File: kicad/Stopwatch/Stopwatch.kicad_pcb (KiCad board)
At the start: 2 copper layers, 13 parts, among them U1 74HC14, U3 SC56-11GWA, U4 SC56-11GWA, U5 SC56-11GWA, U6 SC56-11GWA

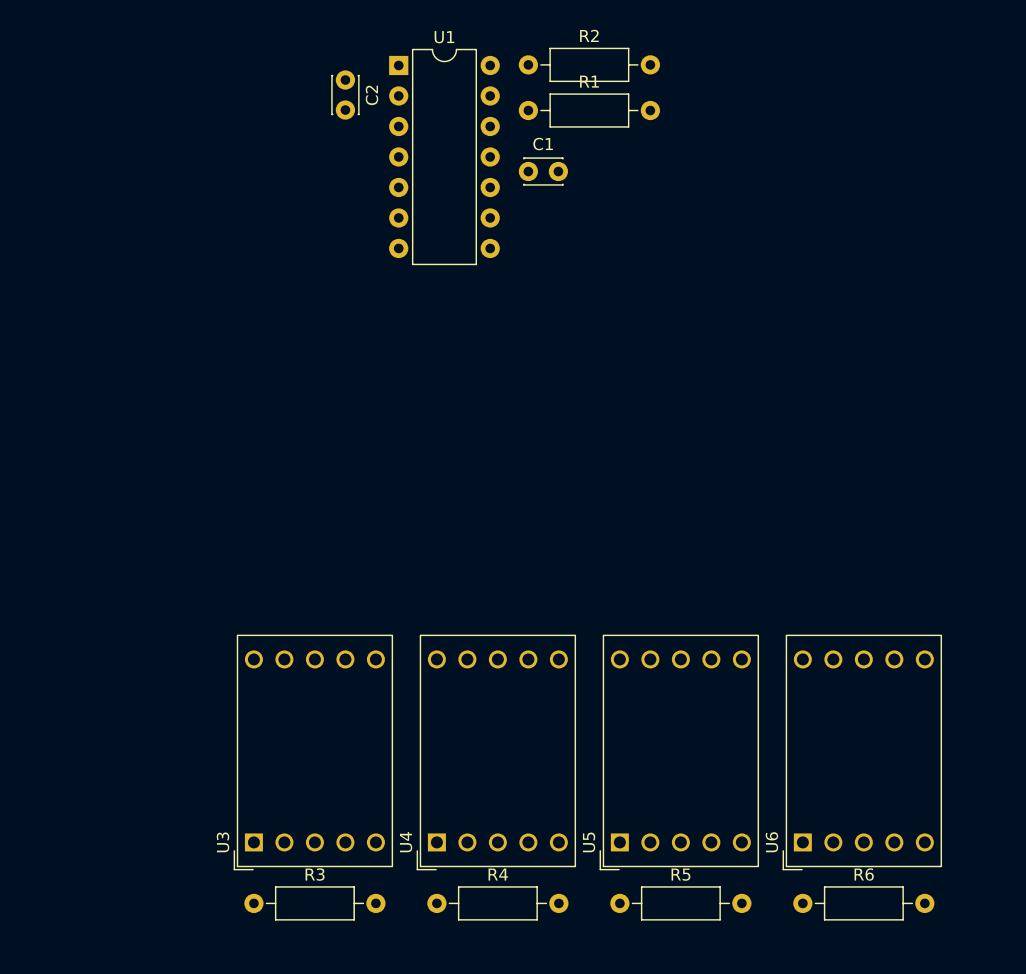
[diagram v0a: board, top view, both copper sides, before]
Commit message: fixed BluePill symbol pin numbers, added button and BluePill footprint
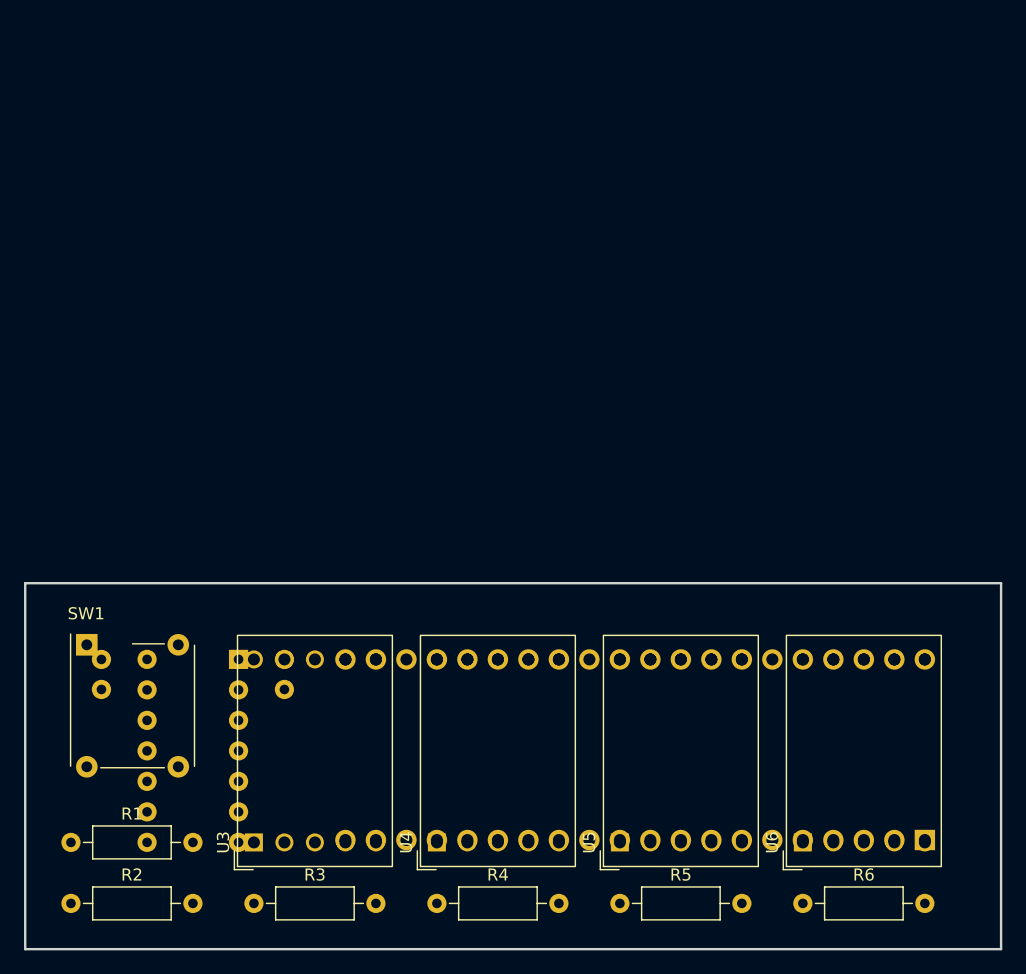
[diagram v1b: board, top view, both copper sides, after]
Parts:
- added SW1: SW_Push, Custom:5ETH935, F.Cu at (76.2, 127.0)
- added U2: BluePill, Custom:BluePill, B.Cu at (118.1, 129.4)
- C1, C2, U1: moved to B.Cu
- moved R2 79.6 mm to (71.1, 142.2)
- moved R1 71.9 mm to (71.1, 137.2)
- moved C1 54.0 mm to (73.7, 121.9), turned to -90 degrees
- moved U1 51.2 mm to (85.1, 121.9), turned to 180 degrees
- moved C2 48.5 mm to (88.9, 121.9)
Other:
- board outline added: 81.3 x 30.5 mm

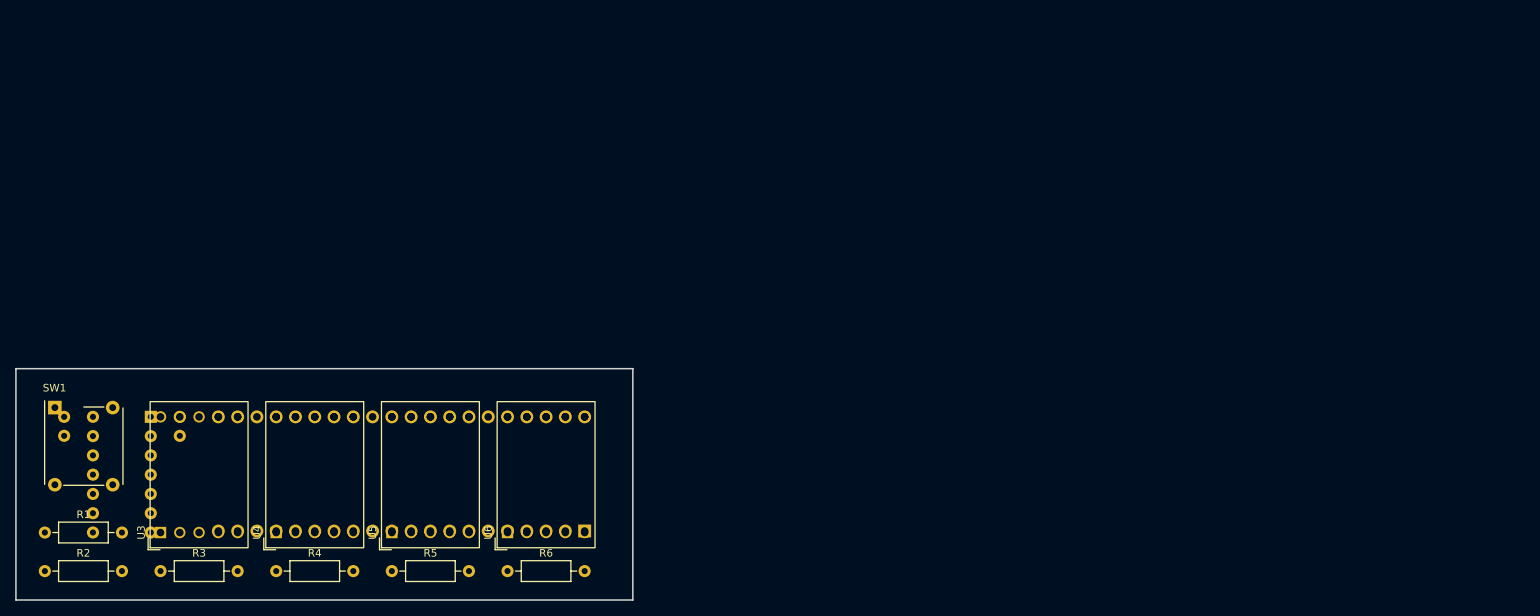
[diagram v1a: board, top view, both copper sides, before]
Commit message: completed pcb design of stopwatch
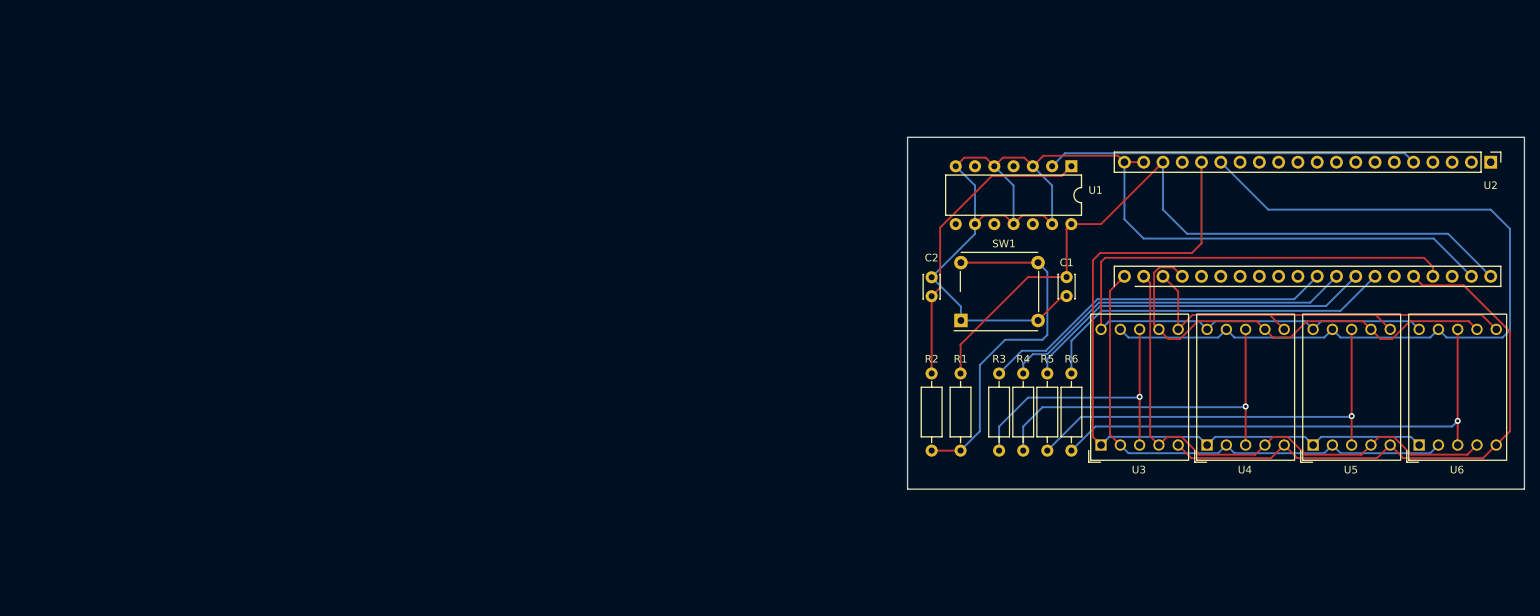
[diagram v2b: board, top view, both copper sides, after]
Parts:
- C1, C2, U1, U2: moved to F.Cu
- moved C1 133.4 mm to (205.7, 103.5)
- moved U1 125.7 mm to (206.4, 88.9), turned to -90 degrees
- moved U3 124.5 mm to (215.4, 118.0)
- moved U2 124.0 mm to (237.5, 95.9), turned to -90 degrees
- moved SW1 123.8 mm to (198.1, 105.5), turned to 90 degrees
- moved U4 123.2 mm to (229.3, 118.0)
- moved R1 122.5 mm to (191.8, 116.2), turned to -90 degrees
- moved U5 121.9 mm to (243.3, 118.0)
- moved U6 120.7 mm to (257.3, 118.0)
- moved R2 119.7 mm to (188.0, 116.2), turned to -90 degrees
- moved R3 111.6 mm to (196.8, 126.4), turned to 90 degrees
- moved C2 100.3 mm to (188.0, 106.0), turned to 90 degrees
- moved R4 99.7 mm to (200.0, 126.4), turned to 90 degrees
- moved R5 87.8 mm to (203.2, 126.4), turned to 90 degrees
- moved R6 76.0 mm to (206.4, 126.4), turned to 90 degrees
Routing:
- net GND: track 0.00 -> 153.9 mm
- net /DISP_C: track 0.00 -> 109.9 mm
- net /DISP_B: track 0.00 -> 99.2 mm
- net +3V3: track 0.00 -> 97.2 mm
- net /DISP_D: track 0.00 -> 95.3 mm
- net /DISP_A: track 0.00 -> 77.6 mm
- net /DISP_F: track 0.00 -> 70.8 mm
- net /DISP_E: track 0.00 -> 68.2 mm
- net Net-(R6-Pad1): track 0.00 -> 67.8 mm, vias 0 -> 1
- net /DISP_DP: track 0.00 -> 59.8 mm
- net /DISP_G: track 0.00 -> 58.0 mm
- net Net-(R5-Pad1): track 0.00 -> 57.9 mm, vias 0 -> 1
- net /TRIG: track 0.00 -> 48.8 mm
- net Net-(R4-Pad1): track 0.00 -> 48.8 mm, vias 0 -> 1
- net /DISP_CC4: track 0.00 -> 47.8 mm
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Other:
- board size 81.3 x 30.5 mm -> 81.3 x 46.4 mm
